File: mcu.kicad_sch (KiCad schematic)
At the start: 1 part, among them U3 STM32F103C8T6

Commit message: update 2021-03-25
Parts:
- added C25, C27: 20pF, symbol Device:C_Small
- added C26, C28: 100nF, symbol Device:C_Small
- added C? (x5): 104, symbol Device:C_Small
- added J1: Conn_01x04, symbol Connector_Generic:Conn_01x04
- added R? (x2): 20R, symbol Device:R_Small
- added R?: 1M, symbol Device:R_Small
- added R?: 4.7K, symbol Device:R_Small
- added U4: XC6206P332MR-G, SOT-23, symbol PMIC-LDO-XC6206P332MR-G_SOT23_:PMIC-LDO-XC6206P332MR-G(SOT23)
- added Y2: 8MHz, symbol Device:Crystal
- added Y3: 32.768KHz, symbol Device:Crystal
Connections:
- net OSC32_IN: now reaches U3.3 (PC14-OSC32_IN)
- net OSC32_OUT: now reaches U3.4 (PC15-OSC32_OUT)
- net OSC_IN: now reaches U3.5 (PD0_OSC_IN)
- net OSC_OUT: now reaches U3.6 (PD1_OSC_OUT)
- new net +3V3: C?.1, J1.1 (Pin_1), U4.2 (VOUT)
- new net +5V: U4.3 (VIN)
- new net GND: C?.2, J1.4 (Pin_4), U4.1 (VSS)
- new net SWCLK: J1.3 (Pin_3)
- new net SWO: J1.2 (Pin_2)
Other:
- note added: "3.3V LDO Regulator"
- note added: "RTC Crystal"
- note added: "Serial Wire Debug"
- note added: "TODO: USB"
- note added: "TODO: hook up I2C lines"
- note added: "TODO: hook up SPI lines"
- note added: "TODO: hook up reset"
- note added: "TODO: hook up switches"

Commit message: hook up STM32
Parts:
- added TP?: TAMPER-RTC, symbol Connector:TestPoint_Small
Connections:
- net SWCLK: now also U3.37 (PA14)
- net SWO: now also U3.34 (PA13)
- net USER_SW_1: now also U3.29 (PA8)
- net USER_SW_2: now also U3.30 (PA9)
- net USER_SW_3: now also U3.31 (PA10)
- net PA0_WKUP: now reaches U3.10 (PA0_WKUP)
- net SPI1_CS: now reaches U3.14 (PA4)
- net SPI1_SCK: now reaches U3.15 (PA5)
- net SPI1_MISO: now reaches U3.16 (PA6)
- net SPI1_MOSI: now reaches U3.17 (PA7)
- net ETH_IRQ: now reaches U3.18 (PB0)
- net at U3.2 (PC13-TAMPER-RTC): now also TP?.1
- net BOOT1: now reaches U3.20 (PB2)
- net I2C2_SCL: now reaches U3.21 (PB10)
- net I2C2_SCL: now also U3.22 (PB11)
- net SPI2_CS: now reaches U3.25 (PB12)
- net SPI2_CS: now also U3.26 (PB13), U3.27 (PB14), U3.28 (PB15)
- net USBDM: now reaches U3.32 (PA11)
- net USBDP: now reaches U3.33 (PA12)
- net I2C1_SCL: now reaches U3.42 (PB6)
- net I2C1_SDA: now reaches U3.43 (PB7)
- net BOOT0: now reaches U3.44 (BOOT0)
- net NRST: now reaches U3.7 (NRST)
- no-connect marks 0 -> 11
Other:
- note added: "TODO: hook up reset / boot"
- note added: "TODO: ideal diode"
- note removed: "TODO: hook up I2C lines"
- note removed: "TODO: hook up SPI lines"
- note removed: "TODO: hook up reset"
- moved on the sheet: C?, R?

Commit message: fix some lingering issues
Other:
- company: (none) -> github.com/westrik
- title: (none) -> NA-01 Time Computer
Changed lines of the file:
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@@
 (kicad_sch (version 20201015) (generator eeschema)
   (paper "USLetter")
+  (title_block
+    (title "NA-01 Time Computer")
+    (date "2021-03-26")
+    (rev "B")
+    (company "github.com/westrik")
+    (comment 1 "MFW007")
+  )
   (junction (at 238.76 99.822) (diameter 1.016) (color 0 0 0 0))
   (junction (at 238.76 110.236) (diameter 1.016) (color 0 0 0 0))
@@
     (stroke (width 0) (type solid) (color 0 0 0 0))
   )
+  (wire (pts (xy 35.56 107.95) (xy 46.99 107.95))
+    (stroke (width 0) (type solid) (color 0 0 0 0))
+  )
   (wire (pts (xy 48.26 185.42) (xy 50.8 185.42))
     (stroke (width 0) (type solid) (color 0 0 0 0))
@@
     (effects (font (size 1.27 1.27)) (justify right))
   )
+  (hierarchical_label "RGB_LED" (shape input) (at 35.56 107.95 180)
+    (effects (font (size 1.27 1.27)) (justify right))
+  )

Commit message: fix label assignments and add 2x7 header
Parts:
- J1: footprint (none) -> Connector_PinHeader_2.54mm:PinHeader_1x04_P2.54mm_Vertical
- TP1: renamed from TP?; footprint (none) -> TestPoint:TestPoint_Keystone_5010-5014_Multipurpose
- U4: footprint SOT-23 -> Package_TO_SOT_SMD:SOT-23
- gave numbers to parts that had none: 9
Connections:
- net I2C2_SCL: no longer U3.22 (PB11)
- net SPI2_CS: no longer U3.26 (PB13), U3.27 (PB14), U3.28 (PB15)
- new net I2C2_SDA: U3.22 (PB11)
- new net SPI2_MISO: U3.27 (PB14)
- new net SPI2_MOSI: U3.28 (PB15)
- new net SPI2_SCK: U3.26 (PB13)

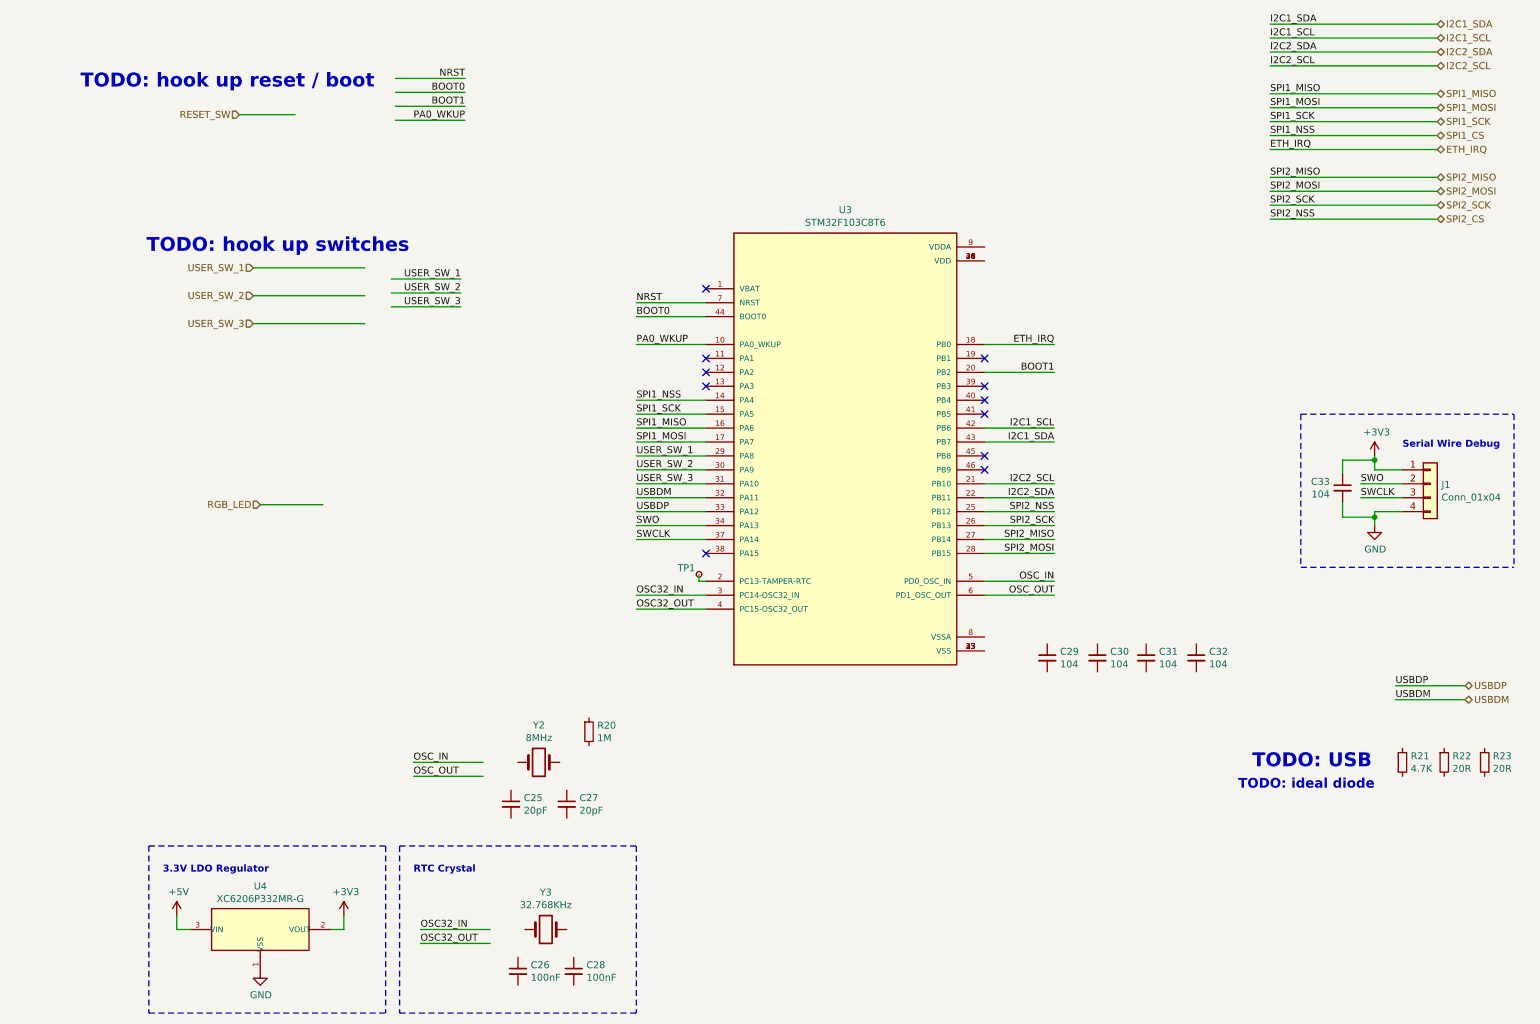
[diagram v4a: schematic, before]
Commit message: finish porting blue pill schematic
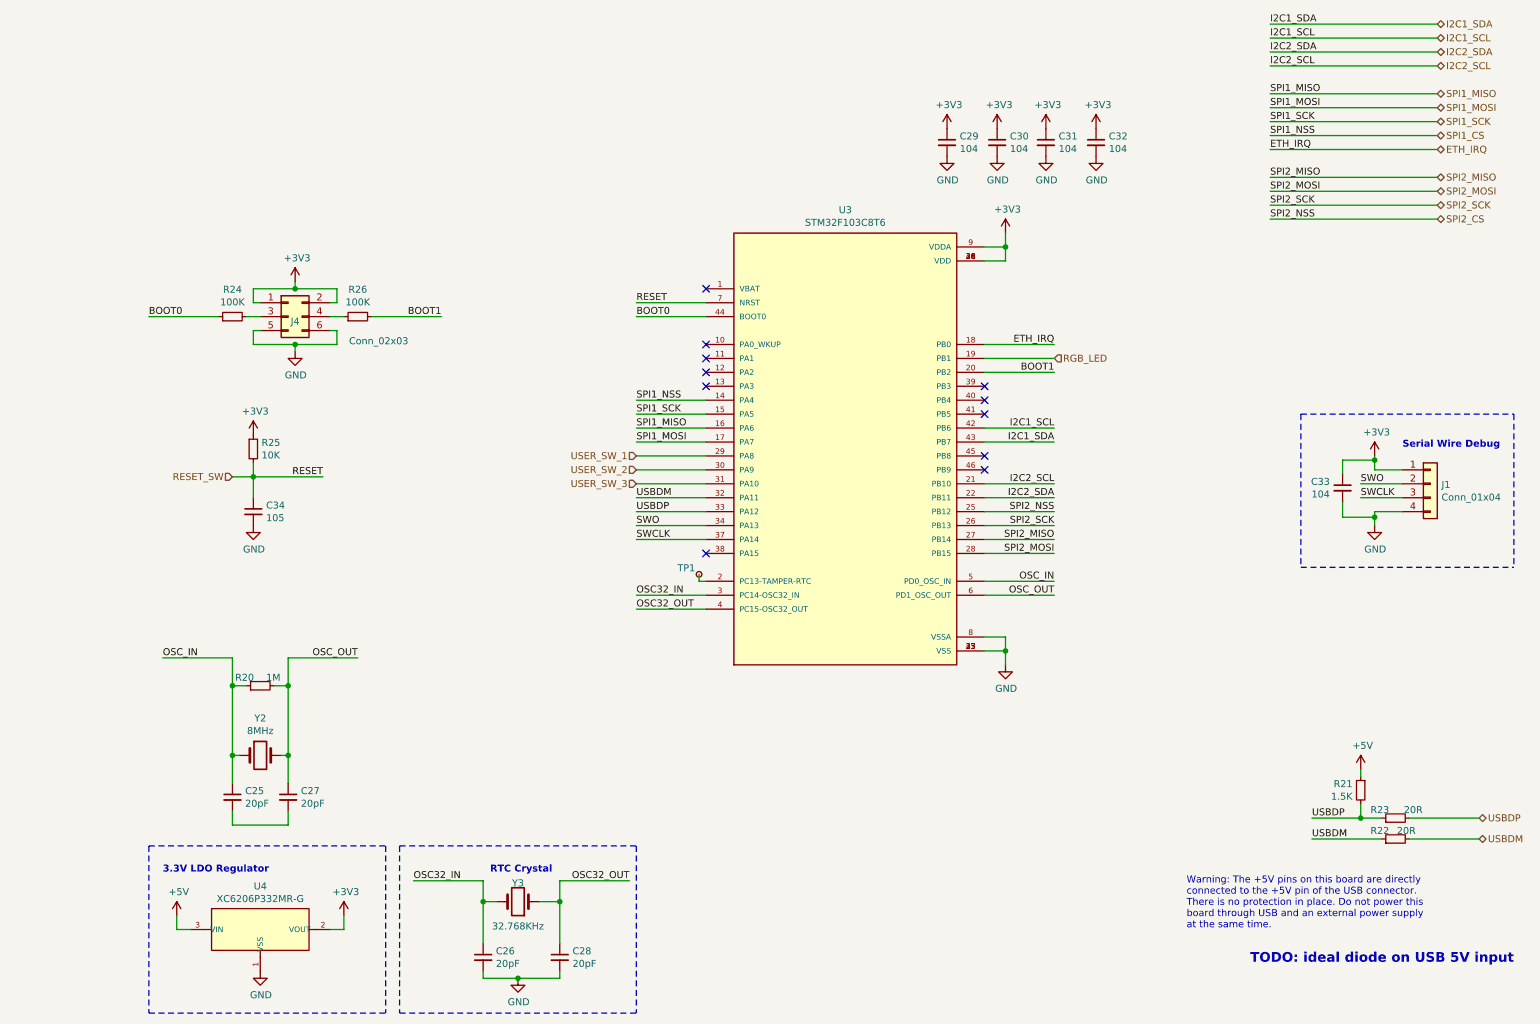
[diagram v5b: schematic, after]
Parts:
- added C34: 105, symbol Device:C_Small
- added J4: Conn_02x03, symbol Connector_Generic:Conn_02x03_Odd_Even
- added R24, R26: 100K, symbol Device:R_Small
- added R25: 10K, symbol Device:R_Small
- C26, C28: value 100nF -> 20pF
- R21: value 4.7K -> 1.5K
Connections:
- net NRST is gone; now on net RESET_SW: U3.7 (NRST)
- net +3V3: now also C29.1, C30.1, C31.1, C32.1, U3.24 (VDD), U3.36 (VDD), U3.48 (VDD), U3.9 (VDDA), J4.1 (Pin_1), J4.2 (Pin_2), R25.1
- net +5V: now also R21.1
- net BOOT0: now also R24.1
- net BOOT1: now also R26.2
- net GND: now also C26.2, C28.2, C29.2, C30.2, C31.2, C32.2, U3.23 (VSS), U3.35 (VSS), U3.47 (VSS), U3.8 (VSSA), C34.2, J4.5 (Pin_5), J4.6 (Pin_6)
- net OSC32_IN: now also C26.1, Y3.2
- net OSC32_OUT: now also C28.1, Y3.1
- net OSC_IN: now also C25.1, R20.1, Y2.1
- net OSC_OUT: now also C27.1, R20.2, Y2.2
- net RESET_SW: now also C34.1, R25.2
- net RGB_LED: now also U3.19 (PB1)
- net USBDM: now also R22.1, R22.2
- net USBDP: now also R21.2, R23.1, R23.2
- net at C25.2: now also C27.2
- net PA0_WKUP: no longer names the net of U3.10 (PA0_WKUP)
- new net: J4.4 (Pin_4), R26.1
- new net: J4.3 (Pin_3), R24.2
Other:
- note added: "TODO: ideal diode on USB 5V input"
- note added: "Warning: The +5V pins on this board are directly connected to the +5V pin of the USB connector. There is no protection in place. Do not power this board through USB and an external power supply at the same time."
- note removed: "TODO: USB"
- note removed: "TODO: hook up reset / boot"
- note removed: "TODO: hook up switches"
- note removed: "TODO: ideal diode"
- moved on the sheet: C25, C26, C27, C28, C29, C30, C31, C32, R20, R21, R22, R23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

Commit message: rough component placement
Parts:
- added C35, C36: 1uF, Capacitor_SMD:C_0402_1005Metric, symbol Device:C_Small
- added R18, R19: 10K, Resistor_SMD:R_0402_1005Metric, symbol Device:R_Small
- C25, C26, C27, C28: footprint (none) -> Capacitor_SMD:C_0402_1005Metric
- C29, C30, C31, C32, C33: value 104 -> 100nF; footprint (none) -> Capacitor_SMD:C_0402_1005Metric
- C34: value 105 -> 1uF; footprint (none) -> Capacitor_SMD:C_0402_1005Metric
- J4: footprint (none) -> Connector_PinHeader_2.54mm:PinHeader_2x03_P2.54mm_Vertical
- R20, R21, R24, R25, R26: footprint (none) -> Resistor_SMD:R_0402_1005Metric
- R22, R23: footprint (none) -> Resistor_SMD:R_0603_1608Metric
- Y2: footprint (none) -> Crystal:Crystal_SMD_5032-2Pin_5.0x3.2mm
- Y3: footprint (none) -> Crystal:Crystal_SMD_3215-2Pin_3.2x1.5mm
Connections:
- net +3V3: now also C36.1, R19.1
- net +5V: now also C35.1
- net GND: now also C25.2, C27.2, C35.2, C36.2, R18.2
- net SWCLK: now also R19.2
- net SWO: now also R18.1
- net NTP_LED: now reaches U3.41 (PB5)
- no-connect marks 11 -> 10
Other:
- moved on the sheet: C25, C27, C29, C31, C32, R20, Y2

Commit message: add some part numbers to schematic
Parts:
- C25, C26, C27, C28: LCSC Part Number (none) -> C1554
- C29, C30, C31, C32, C33: LCSC Part Number (none) -> C1525
- C34, C35, C36: LCSC Part Number (none) -> C52923
- J1, J4, TP1: LCSC Part Number (none) -> N/A
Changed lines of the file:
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@@
+      (effects (font (size 1.27 1.27)) hide)
+    )
+    (property "LCSC Part Number" "N/A" (id 4) (at 115.57 120.65 0)
       (effects (font (size 1.27 1.27)) hide)
     )
@@
       (effects (font (size 1.27 1.27)) hide)
     )
+    (property "LCSC Part Number" "C52923" (id 4) (at 20.32 190.5 0)
+      (effects (font (size 1.27 1.27)) hide)
+    )
   )
   (symbol (lib_id "Device:C_Small") (at 31.75 157.48 0) (unit 1)
@@
       (effects (font (size 1.27 1.27)) hide)
     )
+    (property "LCSC Part Number" "C1554" (id 4) (at 31.75 157.48 0)
+      (effects (font (size 1.27 1.27)) hide)
+    )
   )
   (symbol (lib_id "Device:C_Small") (at 34.29 109.22 0) (unit 1)
@@
       (effects (font (size 1.27 1.27)) hide)
     )
+    (property "LCSC Part Number" "C52923" (id 4) (at 34.29 109.22 0)
+      (effects (font (size 1.27 1.27)) hide)
+    )
   )
   (symbol (lib_id "Device:C_Small") (at 41.91 157.48 0) (unit 1)
@@
       (effects (font (size 1.27 1.27)) hide)
     )
+    (property "LCSC Part Number" "C1554" (id 4) (at 41.91 157.48 0)
+      (effects (font (size 1.27 1.27)) hide)
+    )
   )
   (symbol (lib_id "Device:C_Small") (at 50.8 190.5 0) (mirror y) (unit 1)
@@
       (effects (font (size 1.27 1.27)) hide)
     )
+    (property "LCSC Part Number" "C52923" (id 4) (at 50.8 190.5 0)
+      (effects (font (size 1.27 1.27)) hide)
+    )
   )
   (symbol (lib_id "Device:C_Small") (at 76.2 190.5 0) (unit 1)
@@
       (effects (font (size 1.27 1.27)) hide)
     )
+    (property "LCSC Part Number" "C1554" (id 4) (at 76.2 190.5 0)
+      (effects (font (size 1.27 1.27)) hide)
+    )
   )
   (symbol (lib_id "Device:C_Small") (at 90.17 190.5 0) (unit 1)
@@
       (effects (font (size 1.27 1.27)) hide)
     )
+    (property "LCSC Part Number" "C1554" (id 4) (at 90.17 190.5 0)
+      (effects (font (size 1.27 1.27)) hide)
+    )
   )
   (symbol (lib_id "Device:C_Small") (at 158.75 41.91 0) (unit 1)
@@
       (effects (font (size 1.27 1.27)) hide)
     )
+    (property "LCSC Part Number" "C1525" (id 4) (at 158.75 41.91 0)
+      (effects (font (size 1.27 1.27)) hide)
+    )
   )
   (symbol (lib_id "Device:C_Small") (at 169.926 41.91 0) (unit 1)
@@
       (effects (font (size 1.27 1.27)) hide)
     )
+    (property "LCSC Part Number" "C1525" (id 4) (at 169.926 41.91 0)
+      (effects (font (size 1.27 1.27)) hide)
+    )
   )
   (symbol (lib_id "Device:C_Small") (at 181.61 41.91 0) (unit 1)
@@
       (effects (font (size 1.27 1.27)) hide)
     )
+    (property "LCSC Part Number" "C1525" (id 4) (at 181.61 41.91 0)
+      (effects (font (size 1.27 1.27)) hide)
+    )
   )
   (symbol (lib_id "Device:C_Small") (at 193.294 41.91 0) (unit 1)
@@
       (effects (font (size 1.27 1.27)) hide)
     )
+    (property "LCSC Part Number" "C1525" (id 4) (at 193.294 41.91 0)
+      (effects (font (size 1.27 1.27)) hide)
+    )
   )
   (symbol (lib_id "Device:C_Small") (at 232.918 104.902 0) (mirror y) (unit 1)
@@
     )
     (property "Datasheet" "~" (id 3) (at 232.918 104.902 0)
+      (effects (font (size 1.27 1.27)) hide)
+    )
+    (property "LCSC Part Number" "C1525" (id 4) (at 232.918 104.902 0)
       (effects (font (size 1.27 1.27)) hide)
     )
@@
       (effects (font (size 1.27 1.27)) hide)
     )
+    (property "LCSC Part Number" "N/A" (id 4) (at 248.92 104.14 0)
+      (effects (font (size 1.27 1.27)) hide)
+    )
   )
   (symbol (lib_id "Connector_Generic:Conn_02x03_Odd_Even") (at 40.64 73.66 0) (unit 1)
@@
       (effects (font (size 1.27 1.27)) hide)
     )
+    (property "LCSC Part Number" "N/A" (id 4) (at 40.64 73.66 0)
+      (effects (font (size 1.27 1.27)) hide)
+    )
